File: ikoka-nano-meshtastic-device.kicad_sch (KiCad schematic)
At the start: 8 parts, among them J1 Battery, J2 Solar, J3 Qwiic_RA, Q1 FDN302P, U1 Seeed Studio XIAO nRF52840, U2 E22-900M30S

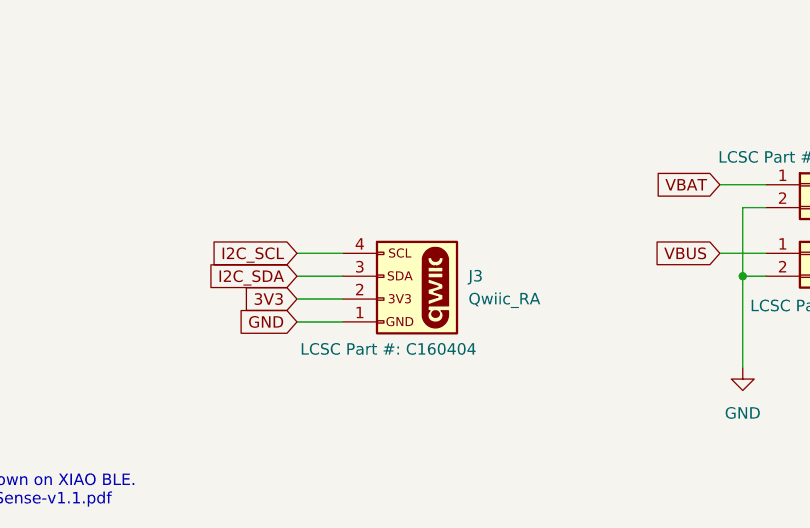
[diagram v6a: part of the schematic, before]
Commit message: Update Seeed XIAO nRF52840 with BAT+ PTH pad
Signed-off-by: Andrew Yong <me@ndoo.sg>
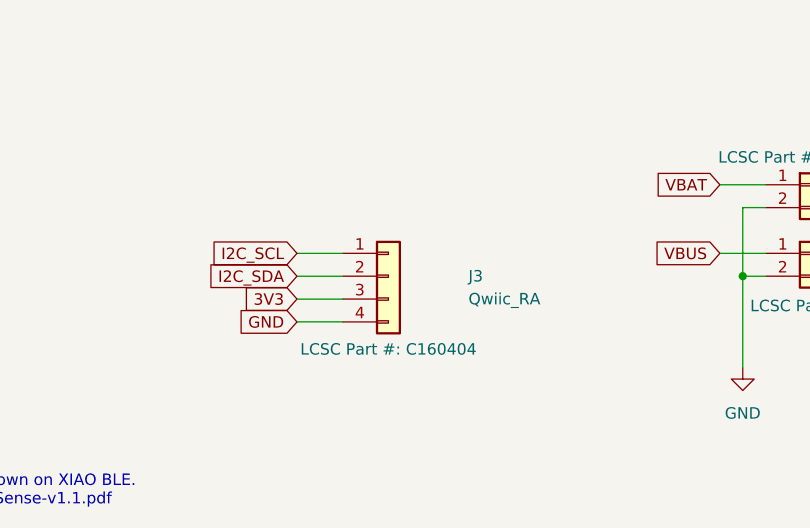
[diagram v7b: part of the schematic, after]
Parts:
- J3: footprint SparkFun-Connector:JST_SMD_1.0mm-4_RA -> Connector_JST:JST_SH_SM04B-SRSS-TB_1x04-1MP_P1.00mm_Horizontal; symbol SparkFun-Connector:Qwiic_Right_Angle -> Connector_Generic:Conn_01x04
- U1: footprint Seeed Studio XIAO Series Library:XIAO-nRF52840-Sense-14P-2.54-21X17.8MM -> Seeed Studio XIAO Series Library:XIAO-nRF52840-BatteryPTH-14P-2.54-21X17.8MM
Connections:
- net 3V3: now also J3.3 (Pin_3); no longer J3.2 (Pin_2)
- net GND: now also J3.4 (Pin_4); no longer J3.1 (Pin_1)
- net I2C_SCL: now also J3.1 (Pin_1); no longer J3.4 (Pin_4)
- net I2C_SDA: now also J3.2 (Pin_2); no longer J3.3 (Pin_3)
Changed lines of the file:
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@@
 	)
 	(symbol
-		(lib_id "SparkFun-Connector:Qwiic_Right_Angle")
+		(lib_id "Connector_Generic:Conn_01x04")
 		(at 180.34 123.19 0)
 		(unit 1)
@@
 			)
 		)
-		(property "Footprint" "SparkFun-Connector:JST_SMD_1.0mm-4_RA"
-			(at 180.34 135.89 0)
-			(effects
-				(font
-					(size 1.27 1.27)
-				)
-				(hide yes)
-			)
-		)
-		(property "Datasheet" "https://www.jst-mfg.com/product/pdf/eng/eSH.pdf"
-			(at 180.34 138.43 0)
-			(effects
-				(font
-					(size 1.27 1.27)
-				)
-				(hide yes)
-			)
-		)
-		(property "Description" ""
+		(property "Footprint" "Connector_JST:JST_SH_SM04B-SRSS-TB_1x04-1MP_P1.00mm_Horizontal"
+			(at 180.34 123.19 0)
+			(effects
+				(font
+					(size 1.27 1.27)
+				)
+				(hide yes)
+			)
+		)
+		(property "Datasheet" "~"
+			(at 180.34 123.19 0)
+			(effects
+				(font
+					(size 1.27 1.27)
+				)
+				(hide yes)
+			)
+		)
+		(property "Description" "Generic connector, single row, 01x04, script generated (kicad-library-utils/schlib/autogen/connector/)"
 			(at 180.34 123.19 0)
 			(effects
@@
 			)
 		)
-		(pin "NC1"
-		)
 		(pin "2"
 		)
 		(pin "4"
-		)
-		(pin "NC2"
 		)
 		(pin "1"
@@
 			)
 		)
-		(property "Footprint" "Seeed Studio XIAO Series Library:XIAO-nRF52840-Sense-14P-2.54-21X17.8MM"
+		(property "Footprint" "Seeed Studio XIAO Series Library:XIAO-nRF52840-BatteryPTH-14P-2.54-21X17.8MM"
 			(at 72.39 54.61 0)
 			(effects

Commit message: Switch back to SparkFun Qwiic symbol/footprint, run DRC, fix 3D models
Signed-off-by: Andrew Yong <me@ndoo.sg>
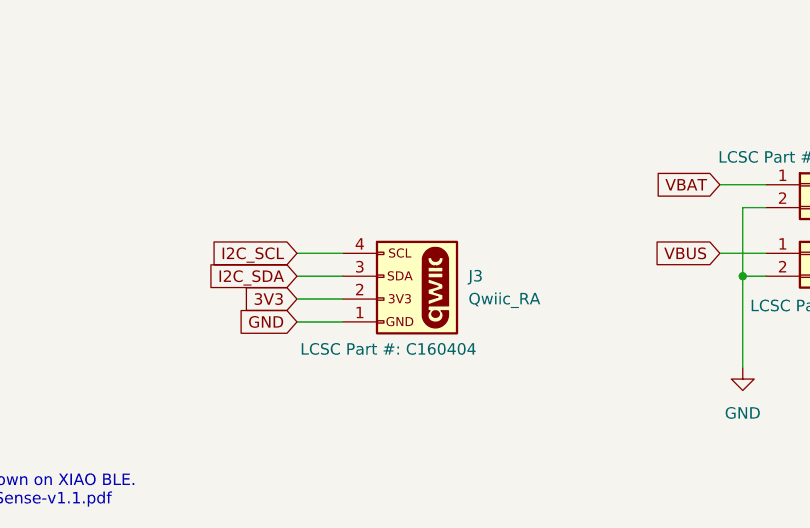
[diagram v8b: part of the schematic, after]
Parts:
- J3: footprint Connector_JST:JST_SH_SM04B-SRSS-TB_1x04-1MP_P1.00mm_Horizontal -> SparkFun-Connector:JST_SMD_1.0mm-4_RA; symbol Connector_Generic:Conn_01x04 -> SparkFun-Connector:Qwiic_Right_Angle
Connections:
- net 3V3: now also J3.2 (Pin_2); no longer J3.3 (Pin_3)
- net GND: now also J3.1 (Pin_1); no longer J3.4 (Pin_4)
- net I2C_SCL: now also J3.4 (Pin_4); no longer J3.1 (Pin_1)
- net I2C_SDA: now also J3.3 (Pin_3); no longer J3.2 (Pin_2)
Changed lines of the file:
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@@
 	)
 	(symbol
-		(lib_id "Connector_Generic:Conn_01x04")
+		(lib_id "SparkFun-Connector:Qwiic_Right_Angle")
 		(at 180.34 123.19 0)
 		(unit 1)
@@
 			)
 		)
-		(property "Footprint" "Connector_JST:JST_SH_SM04B-SRSS-TB_1x04-1MP_P1.00mm_Horizontal"
-			(at 180.34 123.19 0)
+		(property "Footprint" "SparkFun-Connector:JST_SMD_1.0mm-4_RA"
+			(at 180.34 135.89 0)
 			(effects
 				(font
@@
 			)
 		)
-		(property "Datasheet" "~"
-			(at 180.34 123.19 0)
+		(property "Datasheet" "https://www.jst-mfg.com/product/pdf/eng/eSH.pdf"
+			(at 180.34 138.43 0)
 			(effects
 				(font
@@
 			)
 		)
-		(property "Description" "Generic connector, single row, 01x04, script generated (kicad-library-utils/schlib/autogen/connector/)"
-			(at 180.34 123.19 0)
+		(property "Description" "4 pin JST 1mm polarized connector for I2C"
+			(at 180.34 140.97 0)
 			(effects
 				(font
@@
 		(pin "3"
 		)
+		(pin "NC2"
+		)
+		(pin "NC1"
+		)
 		(instances
